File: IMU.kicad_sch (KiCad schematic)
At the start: 8 parts

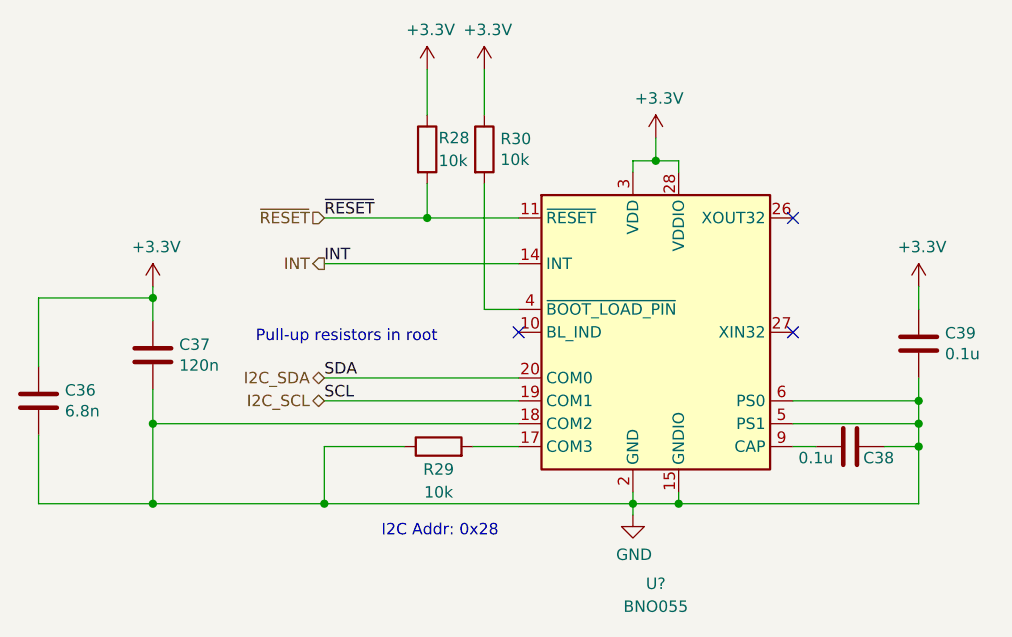
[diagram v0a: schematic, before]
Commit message: bluetooth schematic additions
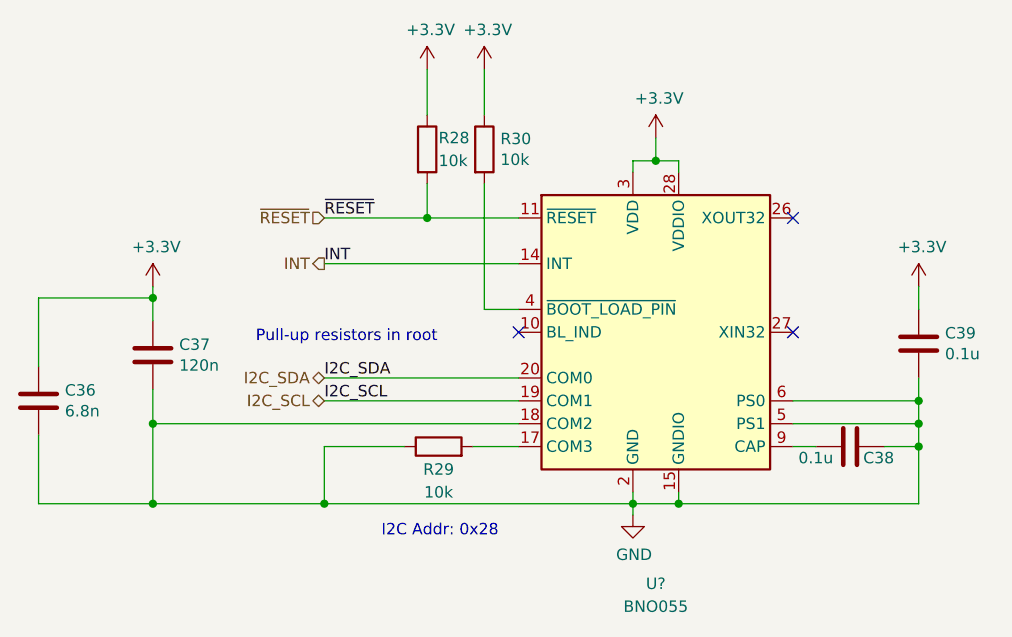
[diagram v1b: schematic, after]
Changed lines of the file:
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@@
     (effects (font (size 1.27 1.27)) (justify left bottom))
   )
-  (label "SCL" (at 123.19 104.14 0) (fields_autoplaced)
+  (label "I2C_SCL" (at 123.19 104.14 0) (fields_autoplaced)
     (effects (font (size 1.27 1.27)) (justify left bottom))
   )
-  (label "SDA" (at 123.19 101.6 0) (fields_autoplaced)
+  (label "I2C_SDA" (at 123.19 101.6 0) (fields_autoplaced)
     (effects (font (size 1.27 1.27)) (justify left bottom))
   )
@@
         )
         (path "/7f2a449b-14af-42b3-8d38-5f0f8a5ee7ce/00000000-0000-0000-0000-00005f6dd18a"
-          (reference "U8") (unit 1)
+          (reference "U6") (unit 1)
         )
       )
@@
   (symbol (lib_id "power:+3.3V") (at 189.23 91.44 0) (unit 1)
     (in_bom yes) (on_board yes) (dnp no)
-    (property "Reference" "#PWR0170" (at 189.23 95.25 0)
+    (property "Reference" "#PWR014" (at 189.23 95.25 0)
       (effects (font (size 1.27 1.27)) hide)
     )
@@
     (instances
       (project "Telemetry-Primary"
-        (path "/7f2a449b-14af-42b3-8d38-5f0f8a5ee7ce/00000000-0000-0000-0000-00005f6d5b75"
-          (reference "#PWR0170") (unit 1)
-        )
         (path "/7f2a449b-14af-42b3-8d38-5f0f8a5ee7ce/00000000-0000-0000-0000-00005f6dd18a"
           (reference "#PWR014") (unit 1)
@@
   (symbol (lib_id "power:+3.3V") (at 134.62 67.31 0) (unit 1)
     (in_bom yes) (on_board yes) (dnp no)
-    (property "Reference" "#PWR0170" (at 134.62 71.12 0)
+    (property "Reference" "#PWR011" (at 134.62 71.12 0)
       (effects (font (size 1.27 1.27)) hide)
     )
@@
     (instances
       (project "Telemetry-Primary"
-        (path "/7f2a449b-14af-42b3-8d38-5f0f8a5ee7ce/00000000-0000-0000-0000-00005f6d5b75"
-          (reference "#PWR0170") (unit 1)
-        )
         (path "/7f2a449b-14af-42b3-8d38-5f0f8a5ee7ce/00000000-0000-0000-0000-00005f6dd18a"
           (reference "#PWR011") (unit 1)
@@
   (symbol (lib_id "power:+3.3V") (at 160.02 74.93 0) (unit 1)
     (in_bom yes) (on_board yes) (dnp no)
-    (property "Reference" "#PWR0170" (at 160.02 78.74 0)
+    (property "Reference" "#PWR013" (at 160.02 78.74 0)
       (effects (font (size 1.27 1.27)) hide)
     )
@@
     (instances
       (project "Telemetry-Primary"
-        (path "/7f2a449b-14af-42b3-8d38-5f0f8a5ee7ce/00000000-0000-0000-0000-00005f6d5b75"
-          (reference "#PWR0170") (unit 1)
-        )
         (path "/7f2a449b-14af-42b3-8d38-5f0f8a5ee7ce/00000000-0000-0000-0000-00005f6dd18a"
           (reference "#PWR013") (unit 1)
@@
   (symbol (lib_id "power:+3.3V") (at 140.97 67.31 0) (unit 1)
     (in_bom yes) (on_board yes) (dnp no)
-    (property "Reference" "#PWR0170" (at 140.97 71.12 0)
+    (property "Reference" "#PWR012" (at 140.97 71.12 0)
       (effects (font (size 1.27 1.27)) hide)
     )
@@
     (instances
       (project "Telemetry-Primary"
-        (path "/7f2a449b-14af-42b3-8d38-5f0f8a5ee7ce/00000000-0000-0000-0000-00005f6d5b75"
-          (reference "#PWR0170") (unit 1)
-        )
         (path "/7f2a449b-14af-42b3-8d38-5f0f8a5ee7ce/00000000-0000-0000-0000-00005f6dd18a"
           (reference "#PWR012") (unit 1)
@@
   (symbol (lib_id "power:+3.3V") (at 104.14 91.44 0) (unit 1)
     (in_bom yes) (on_board yes) (dnp no)
-    (property "Reference" "#PWR0170" (at 104.14 95.25 0)
+    (property "Reference" "#PWR06" (at 104.14 95.25 0)
       (effects (font (size 1.27 1.27)) hide)
     )
@@
     (instances
       (project "Telemetry-Primary"
-        (path "/7f2a449b-14af-42b3-8d38-5f0f8a5ee7ce/00000000-0000-0000-0000-00005f6d5b75"
-          (reference "#PWR0170") (unit 1)
-        )
         (path "/7f2a449b-14af-42b3-8d38-5f0f8a5ee7ce/00000000-0000-0000-0000-00005f6dd18a"
           (reference "#PWR06") (unit 1)
